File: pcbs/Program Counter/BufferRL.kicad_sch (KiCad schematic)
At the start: 2 parts, among them U2001 74HC245, U2002 74HC245

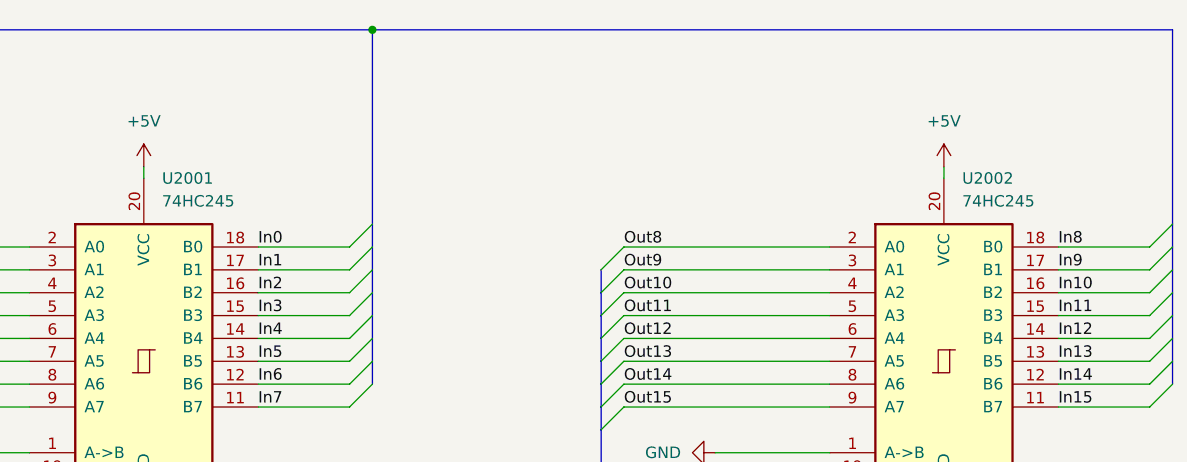
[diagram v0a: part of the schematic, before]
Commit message: Some preliminary routing
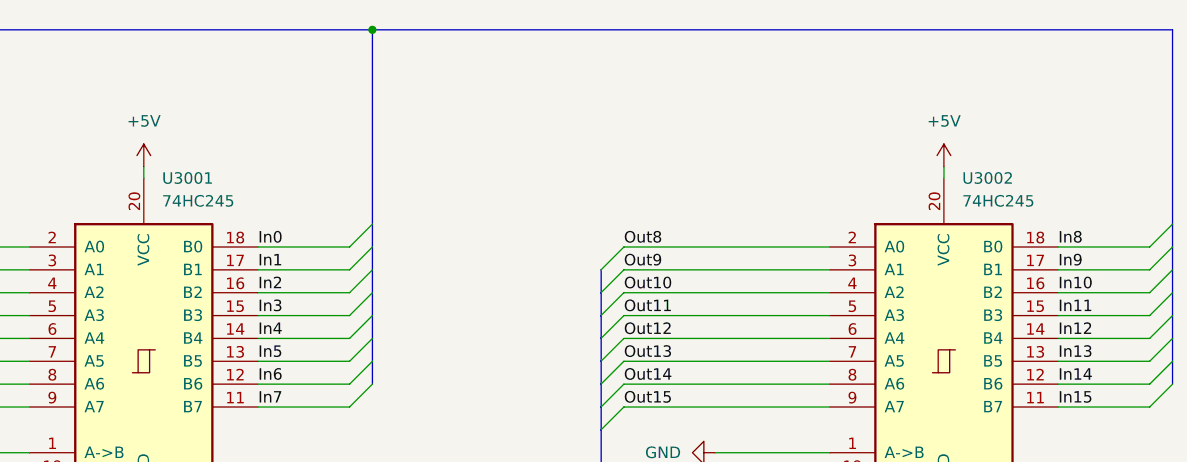
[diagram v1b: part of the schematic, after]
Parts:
- renumbered U2001 to U3001, U2002 to U3002
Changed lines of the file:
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@@
 		(dnp no)
 		(fields_autoplaced yes)
-		(property "Reference" "U2001"
+		(property "Reference" "U3001"
 			(at 115.0494 58.42 0)
 			(effects
@@
 		(dnp no)
 		(fields_autoplaced yes)
-		(property "Reference" "#PWR02002"
+		(property "Reference" "#PWR03002"
 			(at 113.03 60.96 0)
 			(effects
@@
 		(dnp no)
 		(fields_autoplaced yes)
-		(property "Reference" "#PWR02003"
+		(property "Reference" "#PWR03003"
 			(at 113.03 107.95 0)
 			(effects
@@
 		(dnp no)
 		(fields_autoplaced yes)
-		(property "Reference" "#PWR02004"
+		(property "Reference" "#PWR03004"
 			(at 170.18 88.9 0)
 			(effects
@@
 		(dnp no)
 		(fields_autoplaced yes)
-		(property "Reference" "#PWR02001"
+		(property "Reference" "#PWR03001"
 			(at 81.28 88.9 0)
 			(effects
@@
 		(dnp no)
 		(fields_autoplaced yes)
-		(property "Reference" "U2002"
+		(property "Reference" "U3002"
 			(at 203.9494 58.42 0)
 			(effects
@@
 		(dnp no)
 		(fields_autoplaced yes)
-		(property "Reference" "#PWR02006"
+		(property "Reference" "#PWR03006"
 			(at 201.93 107.95 0)
 			(effects
@@
 		(dnp no)
 		(fields_autoplaced yes)
-		(property "Reference" "#PWR02005"
+		(property "Reference" "#PWR03005"
 			(at 201.93 60.96 0)
 			(effects

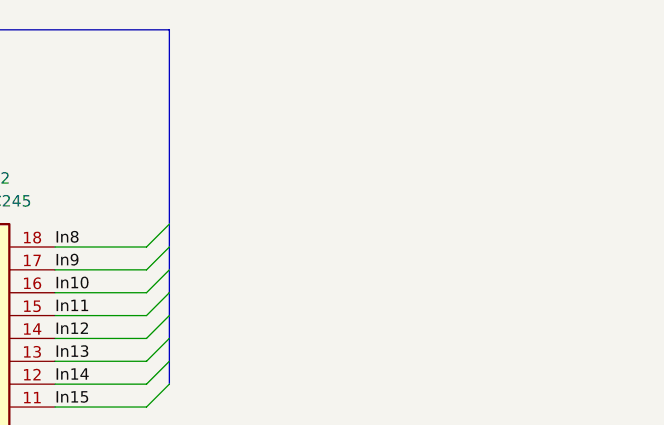
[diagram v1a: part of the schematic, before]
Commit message: Some more LEDs and silkscreening
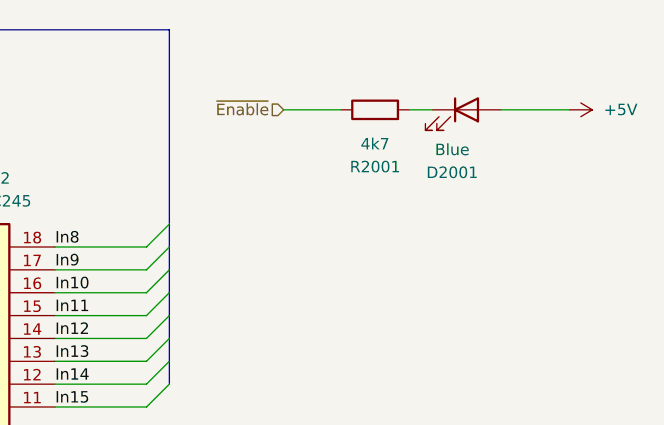
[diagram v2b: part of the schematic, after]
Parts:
- added D2001: Blue, LED_SMD:LED_0603_1608Metric, symbol Device:LED
- added R2001: 4k7, Resistor_SMD:R_0603_1608Metric, symbol Device:R
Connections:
- net +5V: now also D2001.2 (A)
- net ~{Enable}: now also R2001.1
- new net: D2001.1 (K), R2001.2

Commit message: Prepping for final check
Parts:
- renumbered D2001 to D3001, R2001 to R3001
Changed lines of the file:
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@@
 		(dnp no)
 		(fields_autoplaced yes)
-		(property "Reference" "D2001"
+		(property "Reference" "D3001"
 			(at 258.7625 57.785 0)
 			(effects
@@
 		(dnp no)
 		(fields_autoplaced yes)
-		(property "Reference" "#PWR02007"
+		(property "Reference" "#PWR03007"
 			(at 267.97 50.8 0)
 			(effects
@@
 		(dnp no)
 		(fields_autoplaced yes)
-		(property "Reference" "R2001"
+		(property "Reference" "R3001"
 			(at 250.19 57.15 90)
 			(effects
